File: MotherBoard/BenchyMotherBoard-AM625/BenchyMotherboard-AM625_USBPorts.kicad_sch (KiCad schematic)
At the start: 42 parts, among them J4 GSB4116341HR, J5 GSB4116341HR, J6 GSB4116341HR, J7 GSB4116341HR, J8 GSB4116341HR, U16 UCS2114T-1-V/LX, U17 UCS2114T-1-V/LX, U47 AP2171WG-7

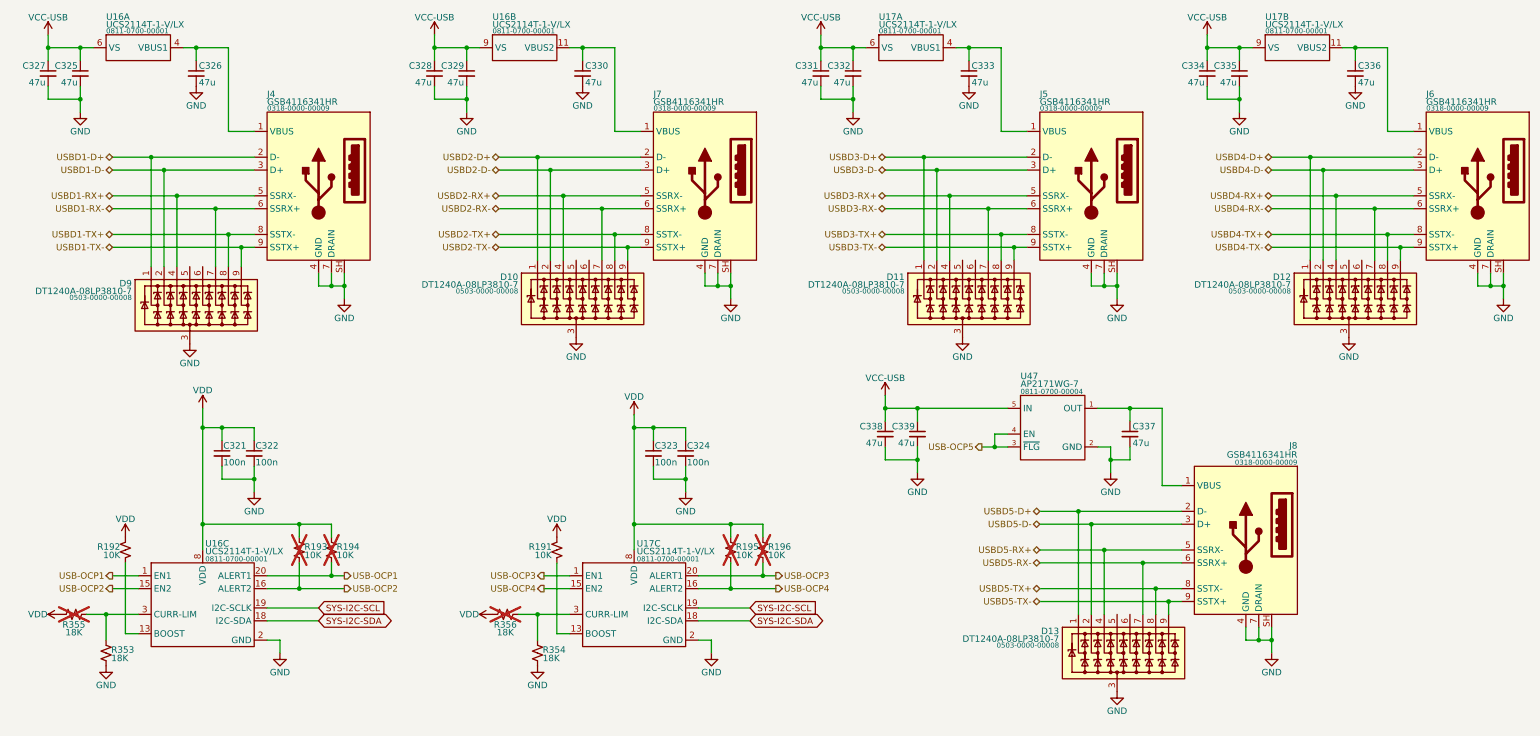
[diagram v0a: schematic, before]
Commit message: Schematic capture mostly complete. Starting PCB layout
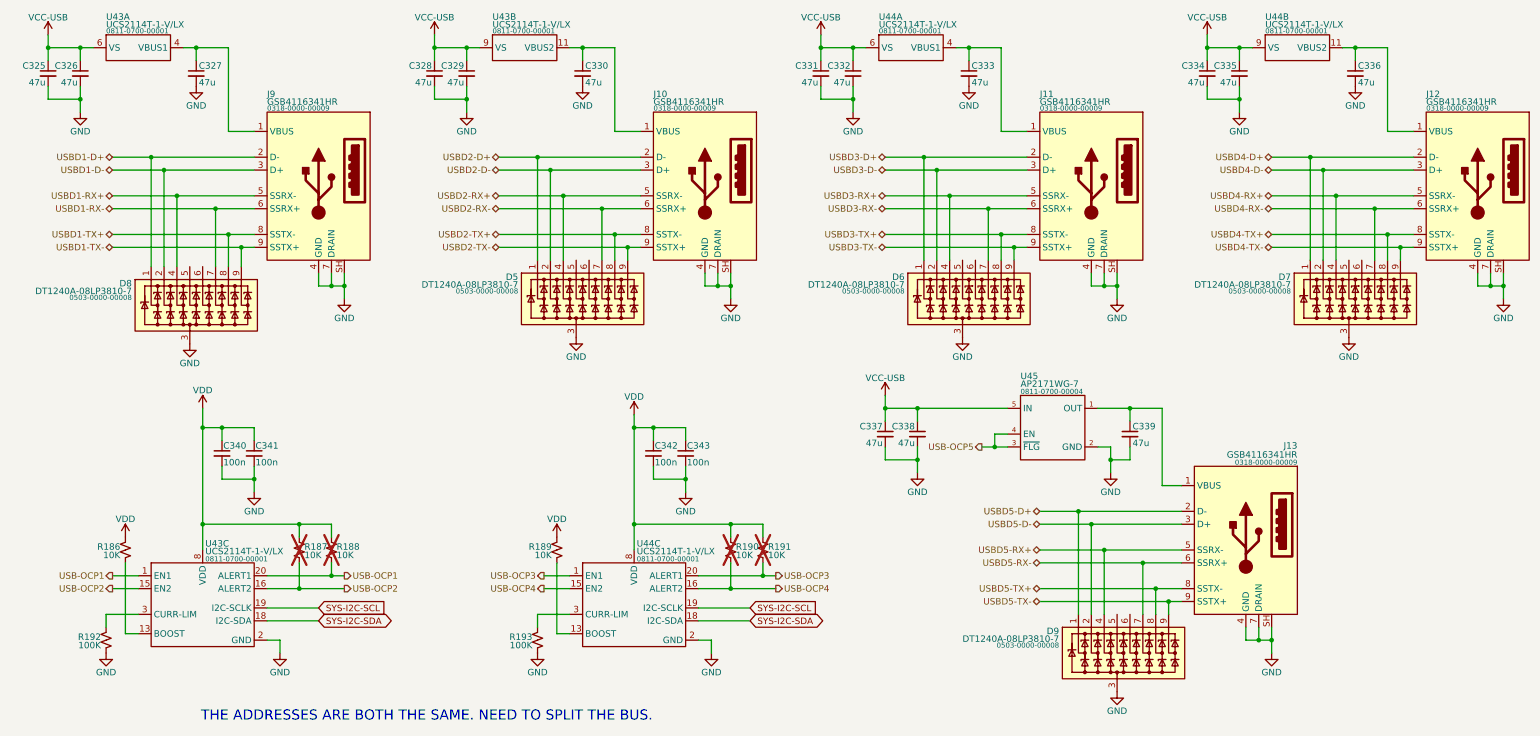
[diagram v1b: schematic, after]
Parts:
- removed R353, R354, R355, R356: 18K, Daxxn_Standard_Resistors:RES_0402, symbol DX_Device:R
- added R192, R193: 100K, Daxxn_Standard_Resistors:RES_0402, symbol DX_Resistor:RMCF0402FT100K
- renumbered C327 to C325, C325 to C326, C326 to C327, C338 to C337, C339 to C338, C337 to C339, C321 to C340, C322 to C341, C323 to C342, C324 to C343, D10 to D5, D11 to D6, D12 to D7, D9 to D8, D13 to D9, J7 to J10, J5 to J11, J6 to J12, J8 to J13, J4 to J9, R192 to R186, R193 to R187, R194 to R188, R191 to R189, R195 to R190, R196 to R191, U16 to U43, U17 to U44, U47 to U45
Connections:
- net GND: now also R192.2, R193.2
- net at U43.3 (COMM-EN): now also R192.1
- net at U44.3 (COMM-EN): now also R193.1
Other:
- note added: "THE ADDRESSES ARE BOTH THE SAME. NEED TO SPLIT THE BUS."
